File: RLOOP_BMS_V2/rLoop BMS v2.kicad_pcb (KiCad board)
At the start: 2 copper layers, 77.5 x 133 mm, 213 parts, among them IC1 FXO-HC736R-1.000, IC2 SN74AUP1G74DCUR, IC3 ATA6870N-PLQW-1, IC4 ATA6870N-PLQW-1, IC5 ATA6870N-PLQW-1, J1 CONN_02X07, J2 2-640387-0, Q1 FDN337N, Q10 PMV20ENR, Q11 PMV20ENR, Q12 PMV20ENR, Q13 PMV20ENR, Q14 PMV20ENR, Q15 PMV20ENR, Q16 PMV20ENR, Q17 PMV20ENR, Q18 PMV20ENR, Q19 PMV20ENR, Q2 PMV20ENR, Q3 PMV20ENR, Q4 PMV20ENR, Q5 PMV20ENR, Q6 PMV20ENR, Q7 PMV20ENR, Q8 PMV20ENR, Q9 PMV20ENR, U1 VOS618A-2X001T

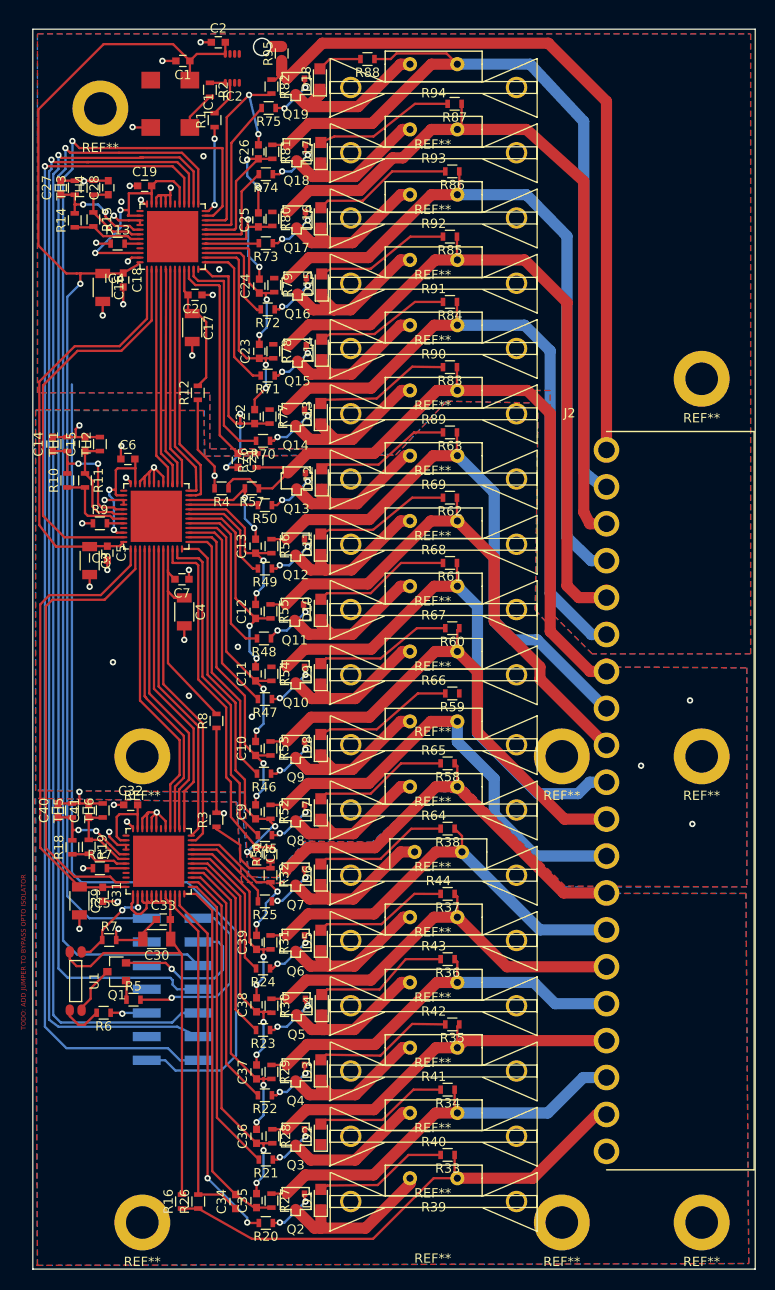
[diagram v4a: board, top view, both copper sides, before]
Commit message: BMS v2 PCB work
almost done, mostly need to check stencil
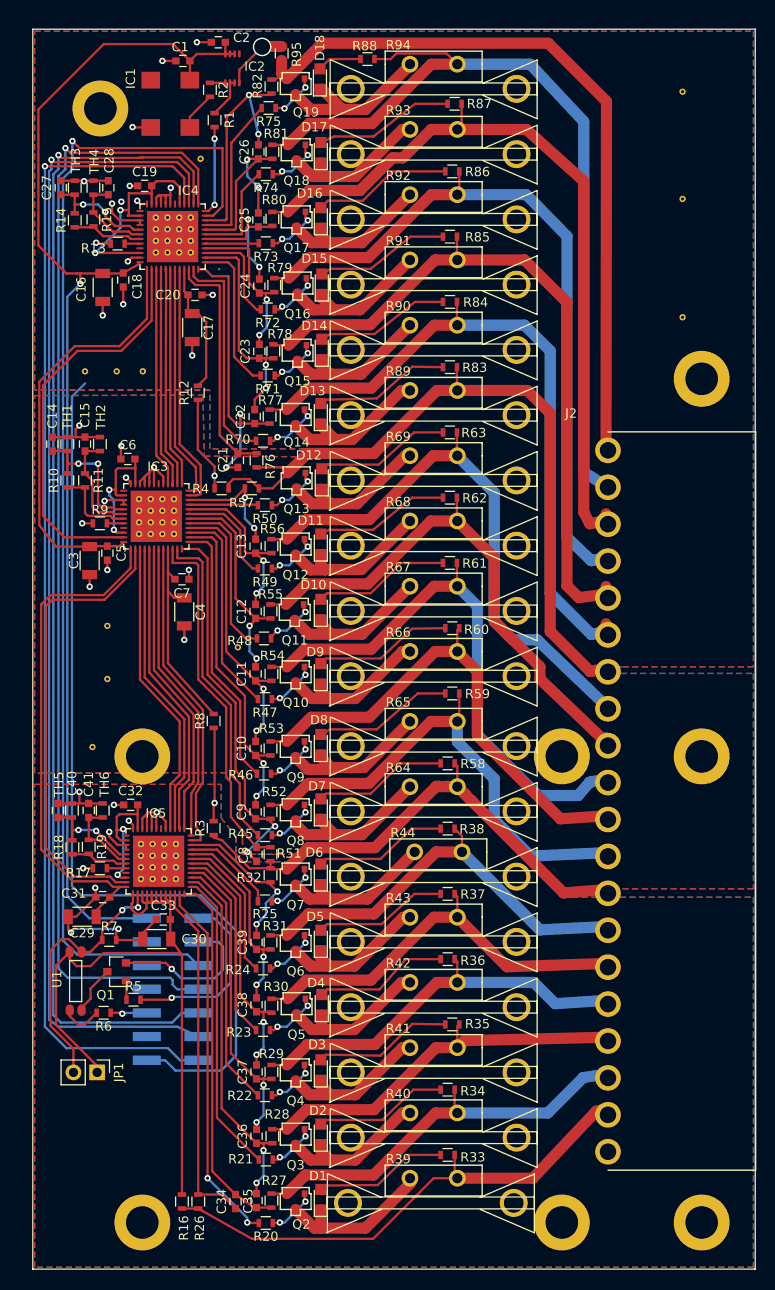
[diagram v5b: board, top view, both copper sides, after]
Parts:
- added JP1: Debug Jumper, Pin_Headers:Pin_Header_Straight_1x02_Pitch2.54mm, F.Cu at (56.9, 154.9)
- added REF**: VIA-.6858mm, rLoop_Footprints:VIA-.6858mm, F.Cu at (67.0, 67.0)
- added REF**: VIA-.6858mm, rLoop_Footprints:VIA-.6858mm, F.Cu at (65.7, 64.5)
- added REF**: VIA-.6858mm, rLoop_Footprints:VIA-.6858mm, F.Cu at (64.5, 64.5)
- added REF**: VIA-.6858mm, rLoop_Footprints:VIA-.6858mm, F.Cu at (63.2, 64.5)
- added REF**: VIA-.6858mm, rLoop_Footprints:VIA-.6858mm, F.Cu at (67.0, 63.2)
- added REF**: VIA-.6858mm, rLoop_Footprints:VIA-.6858mm, F.Cu at (65.7, 63.2)
- added REF**: VIA-.6858mm, rLoop_Footprints:VIA-.6858mm, F.Cu at (64.5, 63.2)
- added REF**: VIA-.6858mm, rLoop_Footprints:VIA-.6858mm, F.Cu at (63.2, 63.2)
- added REF**: VIA-.6858mm, rLoop_Footprints:VIA-.6858mm, F.Cu at (65.2, 97.2)
- added REF**: VIA-.6858mm, rLoop_Footprints:VIA-.6858mm, F.Cu at (63.9, 97.2)
- added REF**: VIA-.6858mm, rLoop_Footprints:VIA-.6858mm, F.Cu at (62.6, 97.2)
- added REF**: VIA-.6858mm, rLoop_Footprints:VIA-.6858mm, F.Cu at (65.7, 67.0)
- added REF**: VIA-.6858mm, rLoop_Footprints:VIA-.6858mm, F.Cu at (61.4, 97.2)
- added REF**: VIA-.6858mm, rLoop_Footprints:VIA-.6858mm, F.Cu at (65.2, 95.9)
- added REF**: VIA-.6858mm, rLoop_Footprints:VIA-.6858mm, F.Cu at (63.9, 95.9)
- added REF**: VIA-.6858mm, rLoop_Footprints:VIA-.6858mm, F.Cu at (62.6, 95.9)
- added REF**: VIA-.6858mm, rLoop_Footprints:VIA-.6858mm, F.Cu at (61.4, 95.9)
- added REF**: VIA-.6858mm, rLoop_Footprints:VIA-.6858mm, F.Cu at (65.2, 94.7)
- added REF**: VIA-.6858mm, rLoop_Footprints:VIA-.6858mm, F.Cu at (63.9, 94.7)
- added REF**: VIA-.6858mm, rLoop_Footprints:VIA-.6858mm, F.Cu at (62.6, 94.7)
- added REF**: VIA-.6858mm, rLoop_Footprints:VIA-.6858mm, F.Cu at (61.4, 94.7)
- added REF**: VIA-.6858mm, rLoop_Footprints:VIA-.6858mm, F.Cu at (65.2, 93.4)
- added REF**: VIA-.6858mm, rLoop_Footprints:VIA-.6858mm, F.Cu at (64.5, 67.0)
- added REF**: VIA-.6858mm, rLoop_Footprints:VIA-.6858mm, F.Cu at (63.9, 93.4)
- added REF**: VIA-.6858mm, rLoop_Footprints:VIA-.6858mm, F.Cu at (62.6, 93.4)
- added REF**: VIA-.6858mm, rLoop_Footprints:VIA-.6858mm, F.Cu at (61.4, 93.4)
- added REF**: VIA-.6858mm, rLoop_Footprints:VIA-.6858mm, F.Cu at (65.3, 134.2)
- added REF**: VIA-.6858mm, rLoop_Footprints:VIA-.6858mm, F.Cu at (64.1, 134.2)
- added REF**: VIA-.6858mm, rLoop_Footprints:VIA-.6858mm, F.Cu at (62.9, 134.2)
- added REF**: VIA-.6858mm, rLoop_Footprints:VIA-.6858mm, F.Cu at (61.6, 134.2)
- added REF**: VIA-.6858mm, rLoop_Footprints:VIA-.6858mm, F.Cu at (65.3, 132.9)
- added REF**: VIA-.6858mm, rLoop_Footprints:VIA-.6858mm, F.Cu at (64.1, 132.9)
- added REF**: VIA-.6858mm, rLoop_Footprints:VIA-.6858mm, F.Cu at (62.9, 132.9)
- added REF**: VIA-.6858mm, rLoop_Footprints:VIA-.6858mm, F.Cu at (63.2, 67.0)
- added REF**: VIA-.6858mm, rLoop_Footprints:VIA-.6858mm, F.Cu at (61.6, 132.9)
- added REF**: VIA-.6858mm, rLoop_Footprints:VIA-.6858mm, F.Cu at (65.3, 131.7)
- added REF**: VIA-.6858mm, rLoop_Footprints:VIA-.6858mm, F.Cu at (64.1, 131.7)
- added REF**: VIA-.6858mm, rLoop_Footprints:VIA-.6858mm, F.Cu at (62.9, 131.7)
- added REF**: VIA-.6858mm, rLoop_Footprints:VIA-.6858mm, F.Cu at (61.6, 131.7)
- added REF**: VIA-.6858mm, rLoop_Footprints:VIA-.6858mm, F.Cu at (65.3, 130.4)
- added REF**: VIA-.6858mm, rLoop_Footprints:VIA-.6858mm, F.Cu at (64.1, 130.4)
- added REF**: VIA-.6858mm, rLoop_Footprints:VIA-.6858mm, F.Cu at (62.9, 130.4)
- added REF**: VIA-.6858mm, rLoop_Footprints:VIA-.6858mm, F.Cu at (61.6, 130.4)
- added REF**: VIA-.6858mm, rLoop_Footprints:VIA-.6858mm, F.Cu at (119.7, 73.9)
- added REF**: VIA-.6858mm, rLoop_Footprints:VIA-.6858mm, F.Cu at (67.0, 65.7)
- added REF**: VIA-.6858mm, rLoop_Footprints:VIA-.6858mm, F.Cu at (119.7, 61.2)
- added REF**: VIA-.6858mm, rLoop_Footprints:VIA-.6858mm, F.Cu at (119.7, 49.7)
- added REF**: VIA-.6858mm, rLoop_Footprints:VIA-.6858mm, F.Cu at (72.0, 109.3)
- added REF**: VIA-.6858mm, rLoop_Footprints:VIA-.6858mm, F.Cu at (56.4, 120.0)
- added REF**: VIA-.6858mm, rLoop_Footprints:VIA-.6858mm, F.Cu at (58.0, 112.7)
- added REF**: VIA-.6858mm, rLoop_Footprints:VIA-.6858mm, F.Cu at (58.0, 107.0)
- added REF**: VIA-.6858mm, rLoop_Footprints:VIA-.6858mm, F.Cu at (61.8, 79.7)
- added REF**: VIA-.6858mm, rLoop_Footprints:VIA-.6858mm, F.Cu at (59.0, 79.7)
- added REF**: VIA-.6858mm, rLoop_Footprints:VIA-.6858mm, F.Cu at (55.6, 79.7)
- added REF**: VIA-.6858mm, rLoop_Footprints:VIA-.6858mm, F.Cu at (68.0, 56.9)
- added REF**: VIA-.6858mm, rLoop_Footprints:VIA-.6858mm, F.Cu at (65.7, 65.7)
- added REF**: VIA-.6858mm, rLoop_Footprints:VIA-.6858mm, F.Cu at (64.5, 65.7)
- added REF**: VIA-.6858mm, rLoop_Footprints:VIA-.6858mm, F.Cu at (63.2, 65.7)
- added REF**: VIA-.6858mm, rLoop_Footprints:VIA-.6858mm, F.Cu at (67.0, 64.5)
- moved J2 3.80 mm to (111.7, 125.8)
- moved C29 1.73 mm to (55.3, 138.2), turned to 180 degrees
- moved R3 0.95 mm to (69.4, 128.7)
- moved REF** 0.34 mm to (92.7, 168.9)
- moved R8 0.30 mm to (69.4, 117.2)
- moved C31 0.30 mm to (57.5, 136.1), turned to 180 degrees
- moved REF** 0.15 mm to (93.0, 161.9)
- moved REF** 0.15 mm to (93.0, 140.9)
- moved REF** 0.15 mm to (93.0, 133.9)
- moved REF** 0.15 mm to (93.0, 154.9)
- moved REF** 0.15 mm to (93.0, 147.9)
- moved REF** 0.15 mm to (93.0, 70.4)
- moved REF** 0.15 mm to (93.0, 77.4)
- moved REF** 0.15 mm to (93.0, 126.9)
- moved REF** 0.15 mm to (93.0, 112.4)
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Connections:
- IC3 pad THRM: (no net) -> GND_2
- IC4 pad THRM: (no net) -> GND_1
- IC5 pad THRM: (no net) -> GND_3
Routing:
- net /PWR_DN_DISABLE/PWR_DN_BMS: track 10.1 -> 28.6 mm
- net VDDHV_3: track 59.8 -> 75.2 mm
- net GND_3: track 42.4 -> 51.7 mm
- net GND_1: track 129.3 -> 137.7 mm
- net Net-(C32-Pad2): track 8.19 -> 15.1 mm, vias 0 -> 2
- net /CONTROLLER 3/VDDHVM: track 50.3 -> 54.7 mm
- net /DISCHARGE Top/CELL_11: track 49.2 -> 52.6 mm
- net Net-(D2-Pad1): track 15.0 -> 17.1 mm
- net /DISCHARGE Top/CELL_9: track 58.3 -> 60.3 mm
- net /DISCHARGE Top/CELL_5: track 70.5 -> 72.3 mm
- net /DISCHARGE Top/CELL_4: track 74.0 -> 75.7 mm
- net /DISCHARGE Top/CELL_2: track 79.9 -> 81.5 mm
- net /DISCHARGE Top/CELL_3: track 75.6 -> 77.1 mm
- net Net-(D18-Pad1): track 17.1 -> 18.3 mm
- net /Clock Generator/VDD: track 131.5 -> 132.5 mm
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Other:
- board text removed: "TODO: ADD JUMPER TO BYPASS OPTO ISOLATOR"

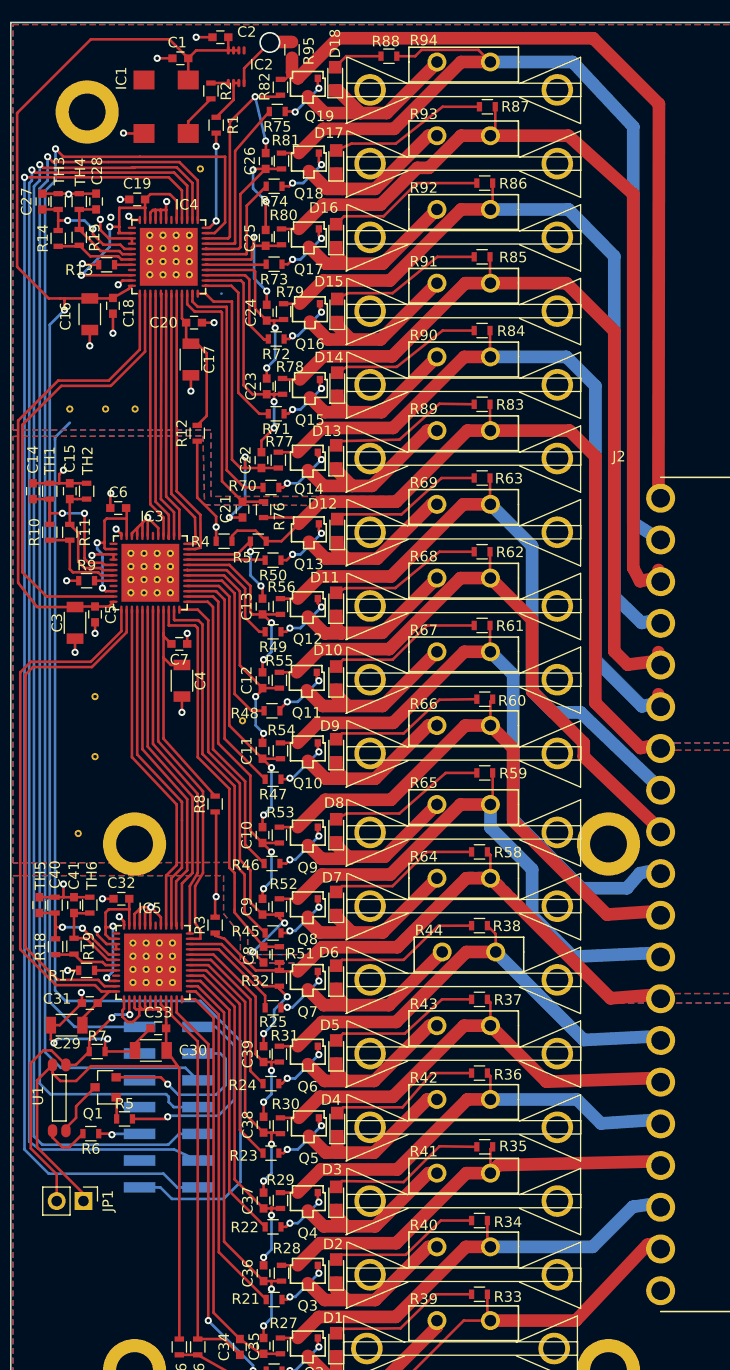
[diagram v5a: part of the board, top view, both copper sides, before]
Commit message: BMS v2 fixed a few traces
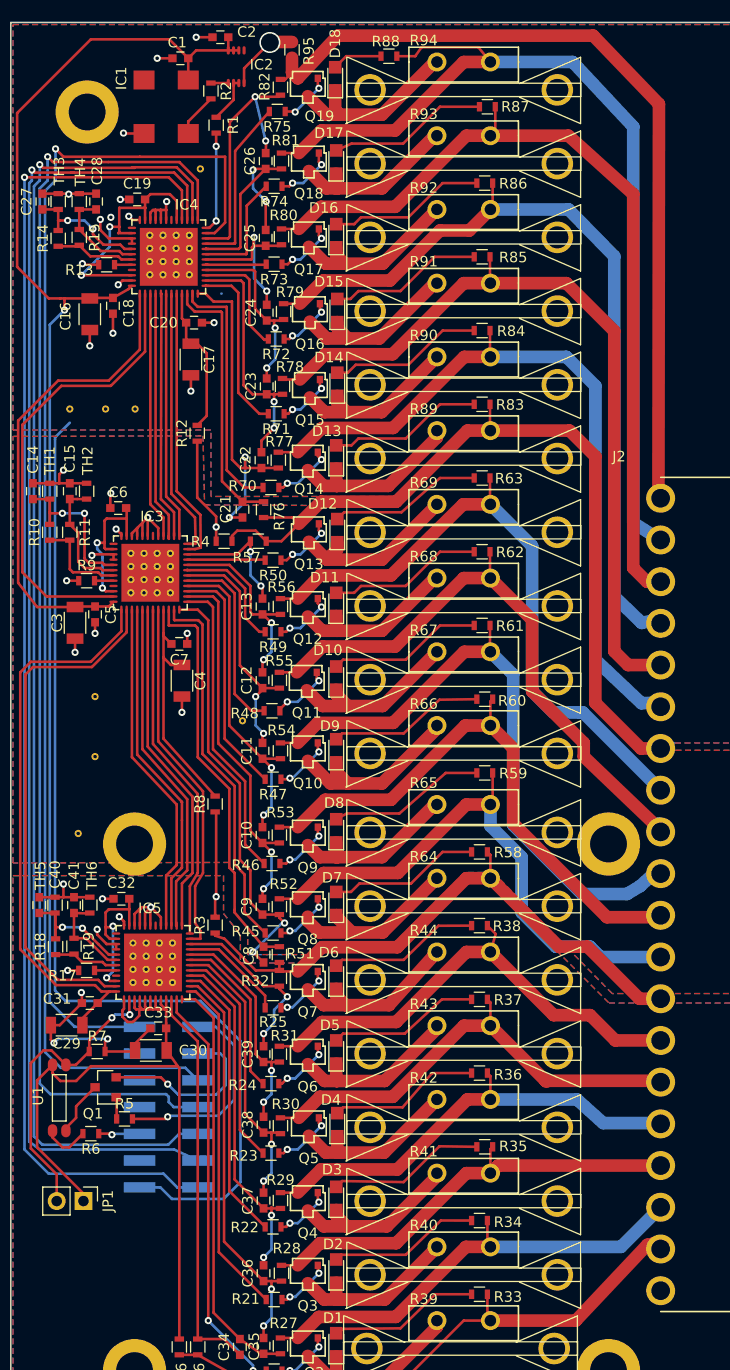
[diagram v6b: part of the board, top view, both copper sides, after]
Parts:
- moved R44 0.50 mm to (93.0, 131.2)
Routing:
- net Net-(D9-Pad1): track 16.9 -> 18.1 mm
- net /DISCHARGE Top/CELL_5: track 72.3 -> 71.3 mm
- net /DISCHARGE Top/CELL_2: track 81.5 -> 80.8 mm
- net Net-(D13-Pad2): track 14.6 -> 15.3 mm
- net /DISCHARGE Top/CELL_9: track 60.3 -> 60.9 mm
- net /DISCHARGE Top/CELL_4: track 75.7 -> 75.1 mm
- net /DISCHARGE Top/CELL_11: track 52.6 -> 53.3 mm
- net Net-(D11-Pad1): track 17.0 -> 16.4 mm
- net /DISCHARGE Top/CELL_7: track 62.2 -> 62.8 mm
- net /DISCHARGE Top/CELL_10: track 54.1 -> 54.6 mm

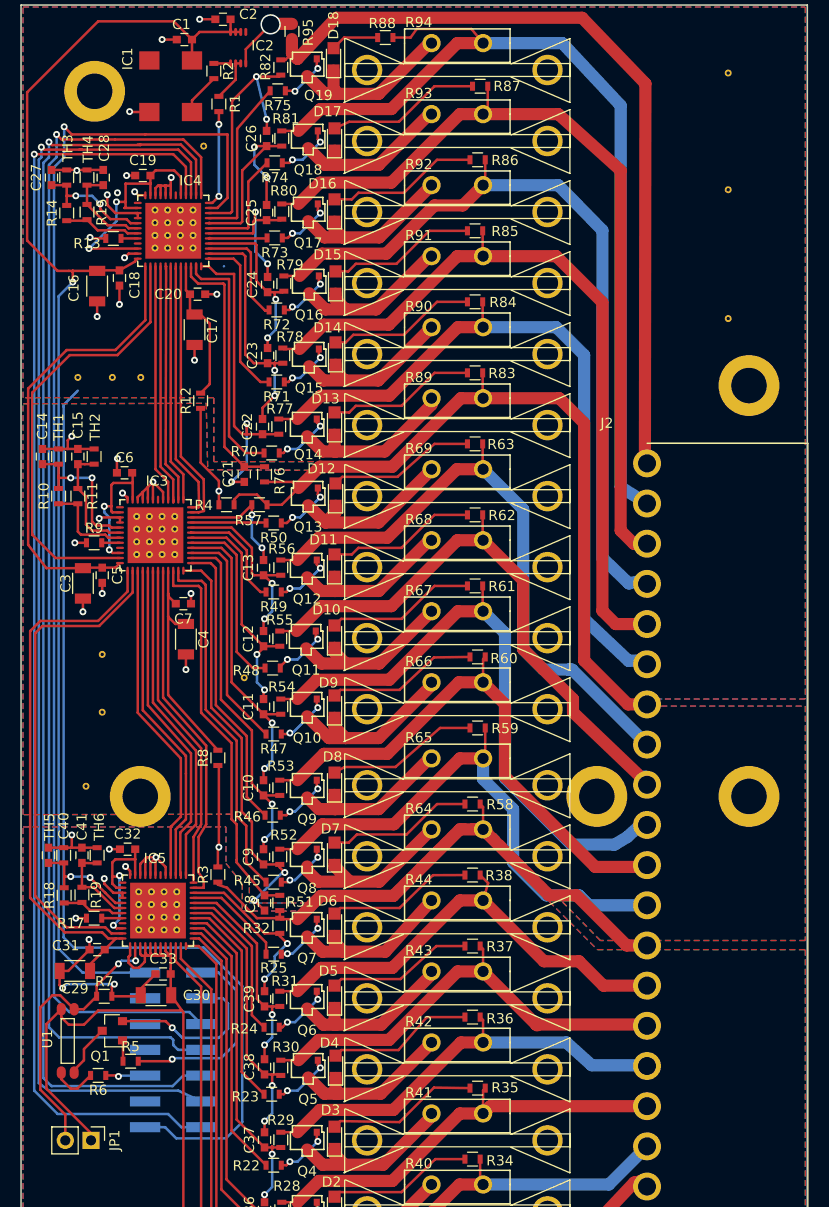
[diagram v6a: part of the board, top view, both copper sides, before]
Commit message: More PCB work on BMS v2
lined up parts with the power node board
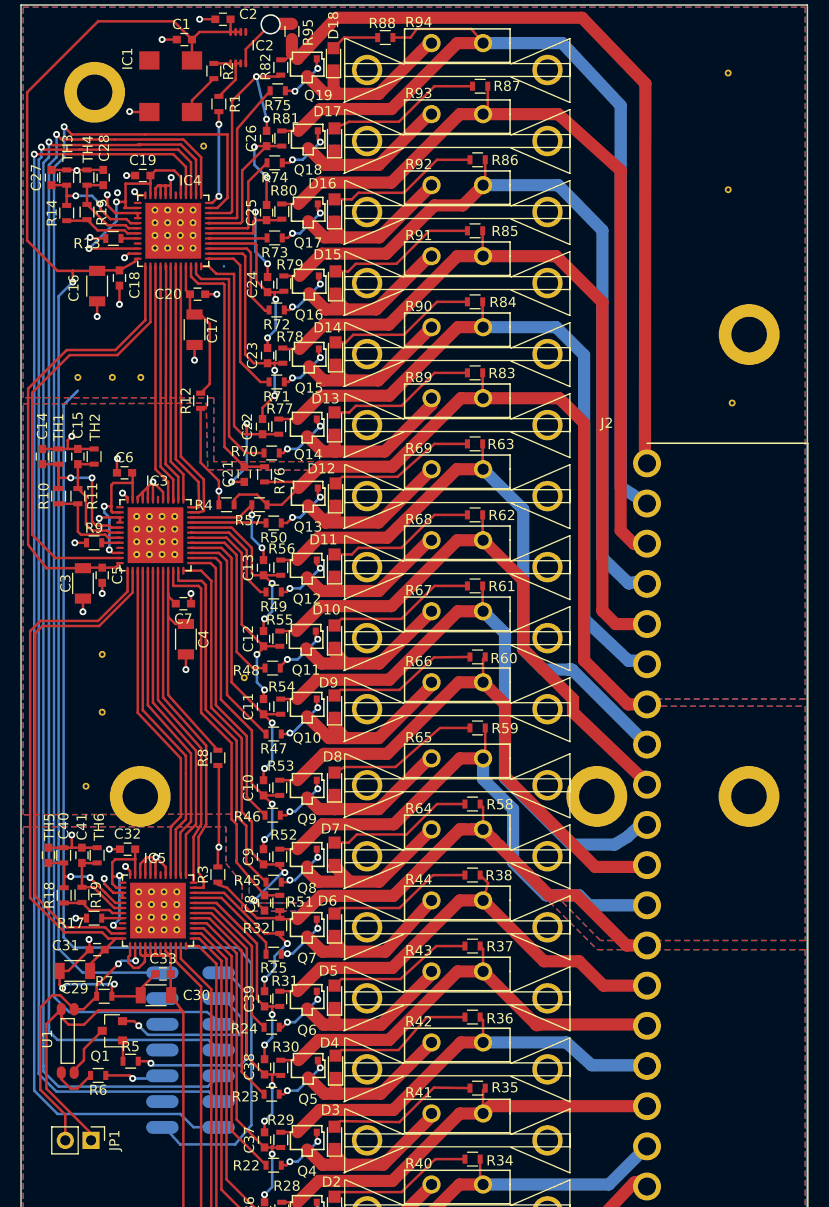
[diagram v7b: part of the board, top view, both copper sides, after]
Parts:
- moved REF** 8.33 mm to (120.1, 82.2)
- moved J1 1.70 mm to (66.7, 146.0)
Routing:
- net /MCU Connector/MOSI_FROM_PWR_NODE: track 127.7 -> 130.3 mm
- net GND_1: track 137.7 -> 140.2 mm
- net MCU_3V3: track 3.95 -> 5.87 mm
- net /MCU Connector/POWER_DN_DISABLE_FROM_PWR_NODE: track 19.7 -> 21.6 mm
- net /Clock Generator/VDD: track 132.8 -> 134.5 mm
- net /MCU Connector/NCS_FROM_PWR_NODE: track 123.5 -> 125.2 mm
- net /MCU Connector/MISO_TO_PWR_NODE: track 128.5 -> 130.2 mm
- net /CONTROLLER 1/IRQ_OUT: track 126.7 -> 128.2 mm
- net /MCU Connector/SCK_FROM_PWR_NODE: track 127.9 -> 129.2 mm
- net MCU_GND: track 16.8 -> 17.4 mm
